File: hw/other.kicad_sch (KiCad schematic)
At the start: 40 parts, among them J2 USB_B, J4 POWER, J5 RESET, U12 NE555P, U2 74HC00, U3 74HC04, U4 74HC02, U8 74HC86, Y1 6MHz

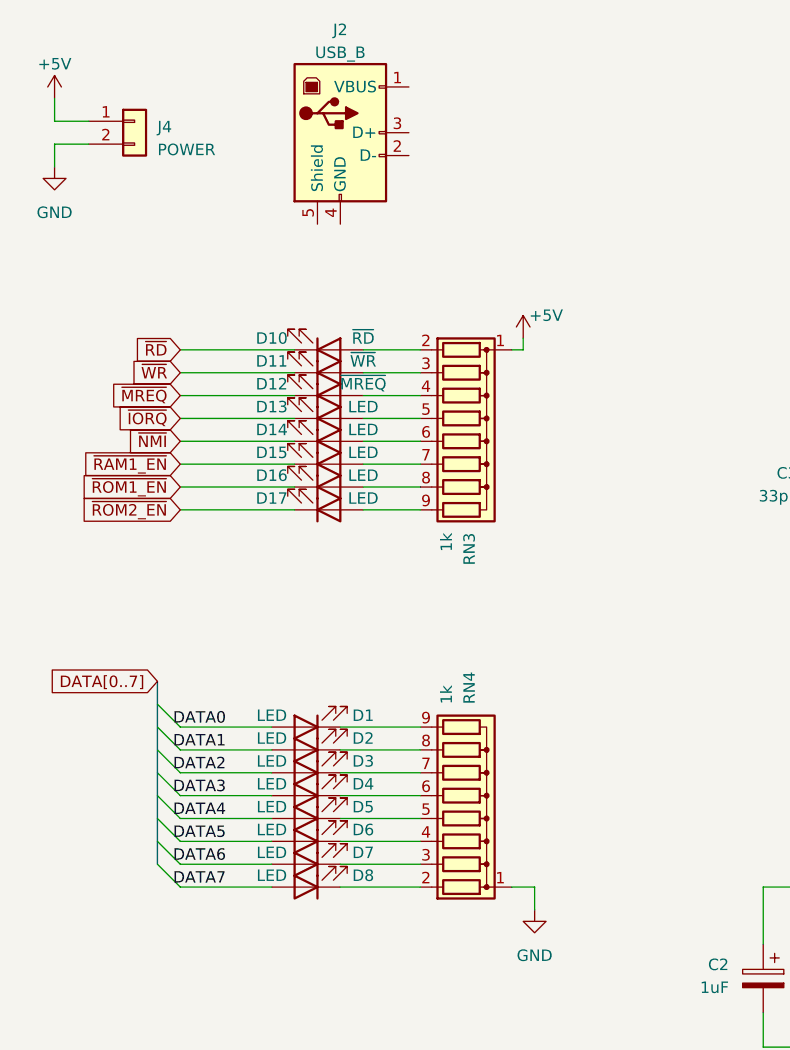
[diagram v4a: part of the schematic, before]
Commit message: Lots of work on Kicad, and gave up on PCB
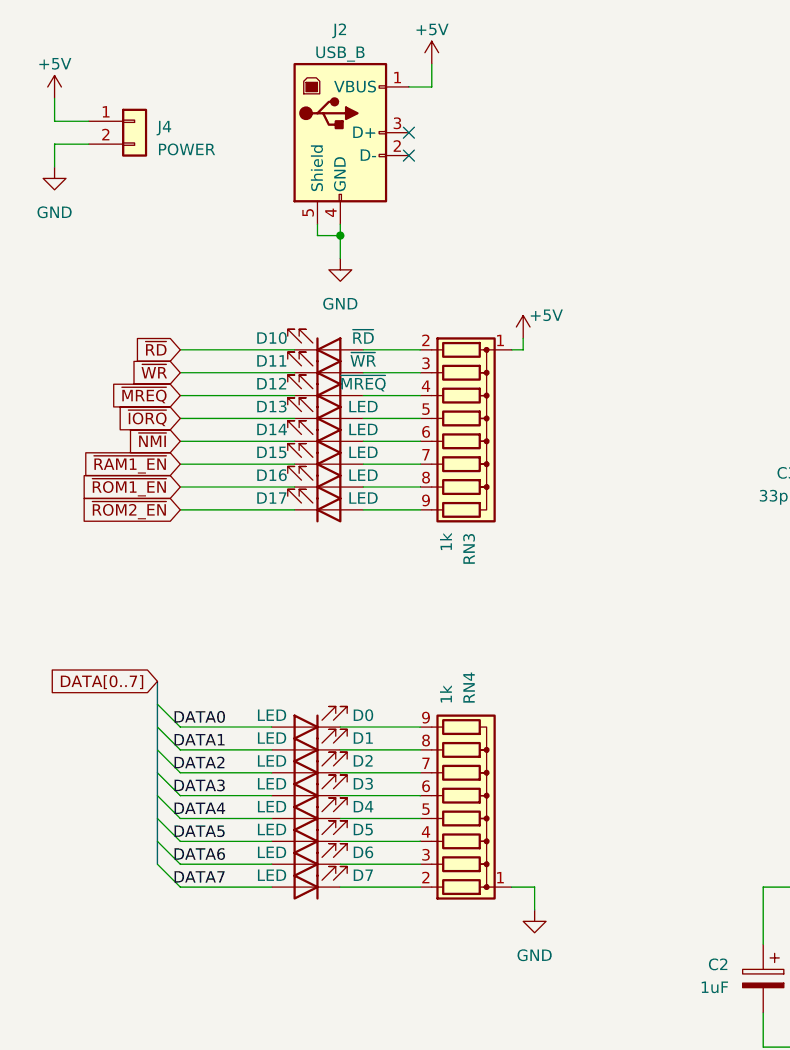
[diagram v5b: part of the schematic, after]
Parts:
- J2: footprint (none) -> Connector_USB:USB_B_OST_USB-B1HSxx_Horizontal
- renumbered D1 to D0, D2 to D1, D3 to D2, D4 to D3, D5 to D4, D6 to D5, D7 to D6, D8 to D7
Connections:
- net +5V: now also J2.1 (VBUS)
- net GND: now also J2.4 (GND), J2.5 (Shield)
- no-connect marks 6 -> 8
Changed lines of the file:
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@@
   (junction (at 135.89 100.33) (diameter 0) (color 0 0 0 0)
+  )
+  (junction (at 49.53 36.83) (diameter 0) (color 0 0 0 0)
   )
   (junction (at 236.22 71.12) (diameter 0) (color 0 0 0 0)
@@
   (no_connect (at 256.54 101.6))
   (no_connect (at 256.54 87.63))
+  (no_connect (at 57.15 25.4))
   (no_connect (at 256.54 73.66))
   (no_connect (at 280.67 34.29))
+  (no_connect (at 57.15 27.94))
   (no_connect (at 256.54 45.72))
   (bus_entry (at 31.75 96.52) (size -2.54 -2.54)
@@
     (stroke (width 0) (type default))
   )
+  (wire (pts (xy 59.69 20.32) (xy 57.15 20.32))
+    (stroke (width 0) (type default))
+  )
   (wire (pts (xy 236.22 90.17) (xy 241.3 90.17))
     (stroke (width 0) (type default))
@@
     (stroke (width 0) (type default))
   )
+  (wire (pts (xy 49.53 36.83) (xy 49.53 35.56))
+    (stroke (width 0) (type default))
+  )
   (wire (pts (xy 123.19 119.38) (xy 119.38 119.38))
     (stroke (width 0) (type default))
@@
     (stroke (width 0) (type default))
   )
+  (wire (pts (xy 46.99 35.56) (xy 46.99 36.83))
+    (stroke (width 0) (type default))
+  )
   (wire (pts (xy 49.53 93.98) (xy 58.42 93.98))
     (stroke (width 0) (type default))
@@
     (stroke (width 0) (type default))
   )
+  (wire (pts (xy 49.53 36.83) (xy 49.53 39.37))
+    (stroke (width 0) (type default))
+  )
   (bus (pts (xy 29.21 99.06) (xy 29.21 101.6))
     (stroke (width 0) (type default))
@@
     (stroke (width 0) (type default))
   )
+  (wire (pts (xy 59.69 17.78) (xy 59.69 20.32))
+    (stroke (width 0) (type default))
+  )
   (wire (pts (xy 41.91 96.52) (xy 31.75 96.52))
     (stroke (width 0) (type default))
@@
   )
   (wire (pts (xy 69.85 49.53) (xy 68.58 49.53))
+    (stroke (width 0) (type default))
+  )
+  (wire (pts (xy 46.99 36.83) (xy 49.53 36.83))
     (stroke (width 0) (type default))
   )
@@
   (symbol (lib_id "z80mgc:LED_3mm") (at 45.72 91.44 180) (unit 1)
     (in_bom yes) (on_board yes) (dnp no)
-    (property "Reference" "D1" (at 52.07 90.17 0)
+    (property "Reference" "D0" (at 52.07 90.17 0)
       (effects (font (size 1.27 1.27)))
     )
@@
       (project "z80mgc"
         (path "/a0755aec-b457-49e5-8300-11792eab574c/0d4dd755-7db3-45ba-b967-0ba9d5a2f689"
-          (reference "D1") (unit 1)
+          (reference "D0") (unit 1)
         )
       )
@@
   (symbol (lib_id "z80mgc:LED_3mm") (at 45.72 99.06 180) (unit 1)
     (in_bom yes) (on_board yes) (dnp no)
-    (property "Reference" "D4" (at 52.07 97.79 0)
+    (property "Reference" "D3" (at 52.07 97.79 0)
       (effects (font (size 1.27 1.27)))
     )
@@
       (project "z80mgc"
         (path "/a0755aec-b457-49e5-8300-11792eab574c/0d4dd755-7db3-45ba-b967-0ba9d5a2f689"
-          (reference "D4") (unit 1)
+          (reference "D3") (unit 1)
         )
       )
@@
     )
   )
+  (symbol (lib_id "power:+5V") (at 59.69 17.78 0) (unit 1)
+    (in_bom yes) (on_board yes) (dnp no) (fields_autoplaced)
+    (property "Reference" "#PWR077" (at 59.69 21.59 0)
+      (effects (font (size 1.27 1.27)) hide)
+    )
+    (property "Value" "+5V" (at 59.69 13.97 0)
+      (effects (font (size 1.27 1.27)))
+    )
+    (property "Footprint" "" (at 59.69 17.78 0)
+      (effects (font (size 1.27 1.27)) hide)
+    )
+    (property "Datasheet" "" (at 59.69 17.78 0)
+      (effects (font (size 1.27 1.27)) hide)
+    )
+    (pin "1")
+    (instances
+      (project "z80mgc"
+        (path "/a0755aec-b457-49e5-8300-11792eab574c/0d4dd755-7db3-45ba-b967-0ba9d5a2f689"
+          (reference "#PWR077") (unit 1)
+        )
+      )
+    )
+  )
   (symbol (lib_id "z80mgc:LED_3mm") (at 48.26 67.31 0) (mirror x) (unit 1)
     (in_bom yes) (on_board yes) (dnp no)
@@
   (symbol (lib_id "z80mgc:LED_3mm") (at 45.72 96.52 180) (unit 1)
     (in_bom yes) (on_board yes) (dnp no)
-    (property "Reference" "D3" (at 52.07 95.25 0)
+    (property "Reference" "D2" (at 52.07 95.25 0)
       (effects (font (size 1.27 1.27)))
     )
@@
       (project "z80mgc"
         (path "/a0755aec-b457-49e5-8300-11792eab574c/0d4dd755-7db3-45ba-b967-0ba9d5a2f689"
-          (reference "D3") (unit 1)
+          (reference "D2") (unit 1)
         )
       )
@@
       (effects (font (size 1.27 1.27)))
     )
-    (property "Footprint" "" (at 53.34 26.67 0)
+    (property "Footprint" "Connector_USB:USB_B_OST_USB-B1HSxx_Horizontal" (at 53.34 26.67 0)
       (effects (font (size 1.27 1.27)) hide)
     )
@@
   (symbol (lib_id "z80mgc:LED_3mm") (at 45.72 101.6 180) (unit 1)
     (in_bom yes) (on_board yes) (dnp no)
-    (property "Reference" "D5" (at 52.07 100.33 0)
+    (property "Reference" "D4" (at 52.07 100.33 0)
       (effects (font (size 1.27 1.27)))
     )
@@
       (project "z80mgc"
         (path "/a0755aec-b457-49e5-8300-11792eab574c/0d4dd755-7db3-45ba-b967-0ba9d5a2f689"
-          (reference "D5") (unit 1)
+          (reference "D4") (unit 1)
         )
       )
@@
   (symbol (lib_id "z80mgc:LED_3mm") (at 45.72 104.14 180) (unit 1)
     (in_bom yes) (on_board yes) (dnp no)
-    (property "Reference" "D6" (at 52.07 102.87 0)
+    (property "Reference" "D5" (at 52.07 102.87 0)
       (effects (font (size 1.27 1.27)))
     )
@@
       (project "z80mgc"
         (path "/a0755aec-b457-49e5-8300-11792eab574c/0d4dd755-7db3-45ba-b967-0ba9d5a2f689"
-          (reference "D6") (unit 1)
+          (reference "D5") (unit 1)
         )
       )
@@
   (symbol (lib_id "z80mgc:LED_3mm") (at 45.72 109.22 180) (unit 1)
     (in_bom yes) (on_board yes) (dnp no)
-    (property "Reference" "D8" (at 52.07 107.95 0)
+    (property "Reference" "D7" (at 52.07 107.95 0)
       (effects (font (size 1.27 1.27)))
     )
@@
       (project "z80mgc"
         (path "/a0755aec-b457-49e5-8300-11792eab574c/0d4dd755-7db3-45ba-b967-0ba9d5a2f689"
-          (reference "D8") (unit 1)
+          (reference "D7") (unit 1)
         )
       )
@@
     )
   )
+  (symbol (lib_id "power:GND") (at 49.53 39.37 0) (unit 1)
+    (in_bom yes) (on_board yes) (dnp no) (fields_autoplaced)
+    (property "Reference" "#PWR076" (at 49.53 45.72 0)
+      (effects (font (size 1.27 1.27)) hide)
+    )
+    (property "Value" "GND" (at 49.53 44.45 0)
+      (effects (font (size 1.27 1.27)))
+    )
+    (property "Footprint" "" (at 49.53 39.37 0)
+      (effects (font (size 1.27 1.27)) hide)
+    )
+    (property "Datasheet" "" (at 49.53 39.37 0)
+      (effects (font (size 1.27 1.27)) hide)
+    )
+    (pin "1")
+    (instances
+      (project "z80mgc"
+        (path "/a0755aec-b457-49e5-8300-11792eab574c/0d4dd755-7db3-45ba-b967-0ba9d5a2f689"
+          (reference "#PWR076") (unit 1)
+        )
+      )
+    )
+  )
   (symbol (lib_id "z80mgc:Capacitor") (at 129.54 64.77 0) (mirror y) (unit 1)
     (in_bom yes) (on_board yes) (dnp no)
@@
   (symbol (lib_id "z80mgc:LED_3mm") (at 45.72 106.68 180) (unit 1)
     (in_bom yes) (on_board yes) (dnp no)
-    (property "Reference" "D7" (at 52.07 105.41 0)
+    (property "Reference" "D6" (at 52.07 105.41 0)
       (effects (font (size 1.27 1.27)))
     )
@@
       (project "z80mgc"
         (path "/a0755aec-b457-49e5-8300-11792eab574c/0d4dd755-7db3-45ba-b967-0ba9d5a2f689"
-          (reference "D7") (unit 1)
+          (reference "D6") (unit 1)
         )
       )
@@
   (symbol (lib_id "z80mgc:LED_3mm") (at 45.72 93.98 180) (unit 1)
     (in_bom yes) (on_board yes) (dnp no)
-    (property "Reference" "D2" (at 52.07 92.71 0)
+    (property "Reference" "D1" (at 52.07 92.71 0)
       (effects (font (size 1.27 1.27)))
     )
@@
       (project "z80mgc"
         (path "/a0755aec-b457-49e5-8300-11792eab574c/0d4dd755-7db3-45ba-b967-0ba9d5a2f689"
-          (reference "D2") (unit 1)
-        )
-      )
+          (reference "D1") (unit 1)
+        )
+      )
